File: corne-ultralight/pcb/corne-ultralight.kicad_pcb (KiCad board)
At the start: 2 copper layers, 275.5 x 105.6 mm, 132 parts, among them J2 OLED, J5 Breakaway_Tabs, J7 OLED, SW1 SW_PUSH, SW10 SW_PUSH, SW11 SW_PUSH, SW12 SW_PUSH, SW13 SW_PUSH, SW14 SW_PUSH, SW15 SW_PUSH, SW16 SW_PUSH, SW17 SW_PUSH, SW18 SW_PUSH, SW19 SW_PUSH, SW2 SW_PUSH, SW20 SW_PUSH, SW21 SW_PUSH, SW22 SW_PUSH, SW23 SW_PUSH, SW24 SW_PUSH, SW25 SW_PUSH, SW26 SW_PUSH, SW27 SW_PUSH, SW28 SW_PUSH, SW29 SW_PUSH, SW3 SW_PUSH, SW30 SW_PUSH, SW31 SW_PUSH, SW32 SW_PUSH, SW33 SW_PUSH, SW34 SW_PUSH, SW35 SW_PUSH, SW36 SW_PUSH, SW37 SW_PUSH, SW38 SW_PUSH, SW39 SW_PUSH, SW4 SW_PUSH, SW40 SW_PUSH, SW41 SW_PUSH, SW42 SW_PUSH, SW5 SW_PUSH, SW6 SW_PUSH, SW7 SW_PUSH, SW8 SW_PUSH, SW9 SW_PUSH, U1 ProMicro, U2 ProMicro

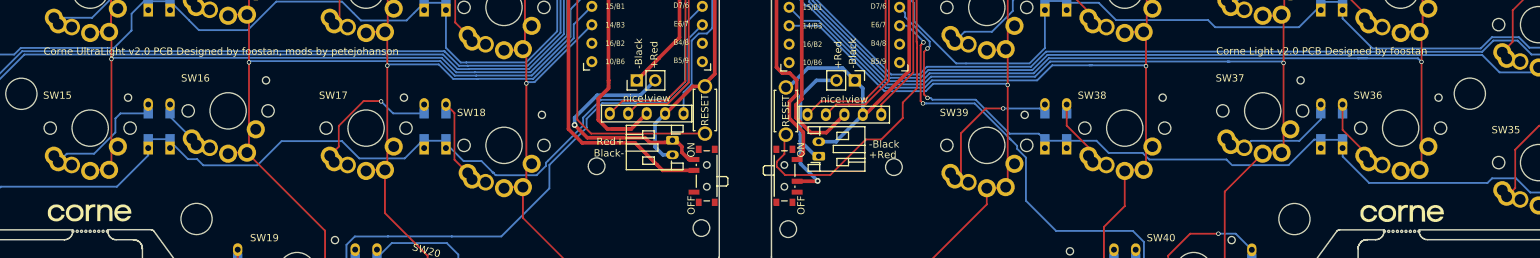
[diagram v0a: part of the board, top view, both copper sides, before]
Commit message: Move components to to the B side
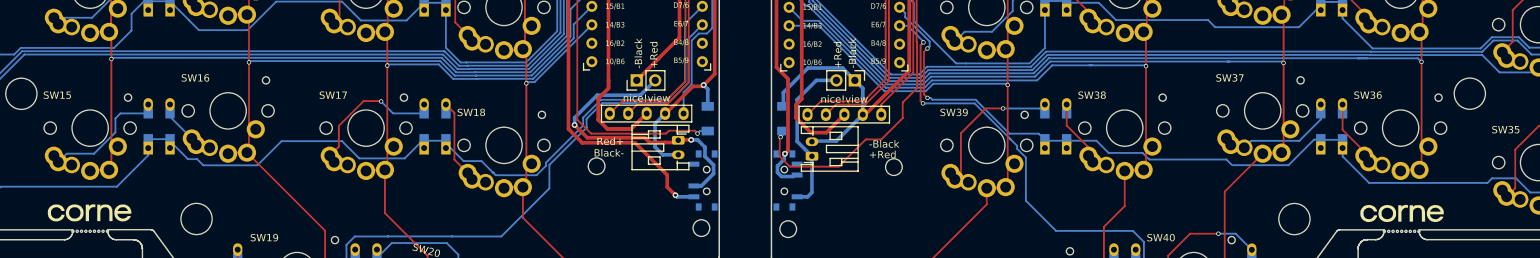
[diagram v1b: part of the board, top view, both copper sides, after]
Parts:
- PSW1, PSW2: moved to B.Cu
- RSW1, RSW2: footprint kbd:ResetSW_1side -> beekeeb_lib:sweep-SW_SPST_B3U-1000P; moved to B.Cu
- moved RSW1 1.26 mm to (145.3, 77.9), turned to 90 degrees
- moved RSW2 1.11 mm to (155.7, 77.9), turned to 90 degrees
- moved BATJ4 0.94 mm to (159.6, 83.0)
- moved BATJ2 0.80 mm to (141.2, 80.8)
- moved PSW1 0.64 mm to (144.8, 86.4), turned to -90 degrees
- moved PSW2 0.64 mm to (156.1, 86.4), turned to 90 degrees
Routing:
- net Net-(BATJ1-Pad2): track 33.1 -> 41.1 mm, vias 1 -> 2
- net GND: track 88.9 -> 92.8 mm, vias 0 -> 1
- net GNDA: track 76.6 -> 80.4 mm
- net +BATTA: track 45.3 -> 48.1 mm, vias 0 -> 1
- net +BATT: track 58.2 -> 60.7 mm, vias 0 -> 1
- net reset_r: track 79.7 -> 77.5 mm, vias 0 -> 1
- net Net-(BATJ3-Pad2): track 24.7 -> 22.9 mm, vias 1 -> 0
- net reset: track 50.1 -> 50.9 mm, vias 0 -> 1
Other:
- board text added: "Corne UltraLight v2.0b designed by foostan mods by petejohanson & beekeeb"
- board text removed: "Corne Light v2.0 PCB Designed by foostan"
- board text removed: "Corne UltraLight v2.0 PCB Designed by foostan, mods by petejohanson"
